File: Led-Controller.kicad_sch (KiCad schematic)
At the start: 68 parts, among them J1 Program, J2 Barrel_Jack, J3 Screw_Terminal, Q1 CSD18540Q5B, Q2 CSD18540Q5B, Q3 CSD18540Q5B, Q4 CSD18540Q5B, Q5 CSD18540Q5B, Q6 CSD18540Q5B, U1 TPS5430DDA, U2 TPS5430DDA, U3 ESP32-WROOM-32E, U4 1ED44175N01BXTSA1, U5 1ED44175N01BXTSA1, U6 1ED44175N01BXTSA1, U7 1ED44175N01BXTSA1, U8 1ED44175N01BXTSA1

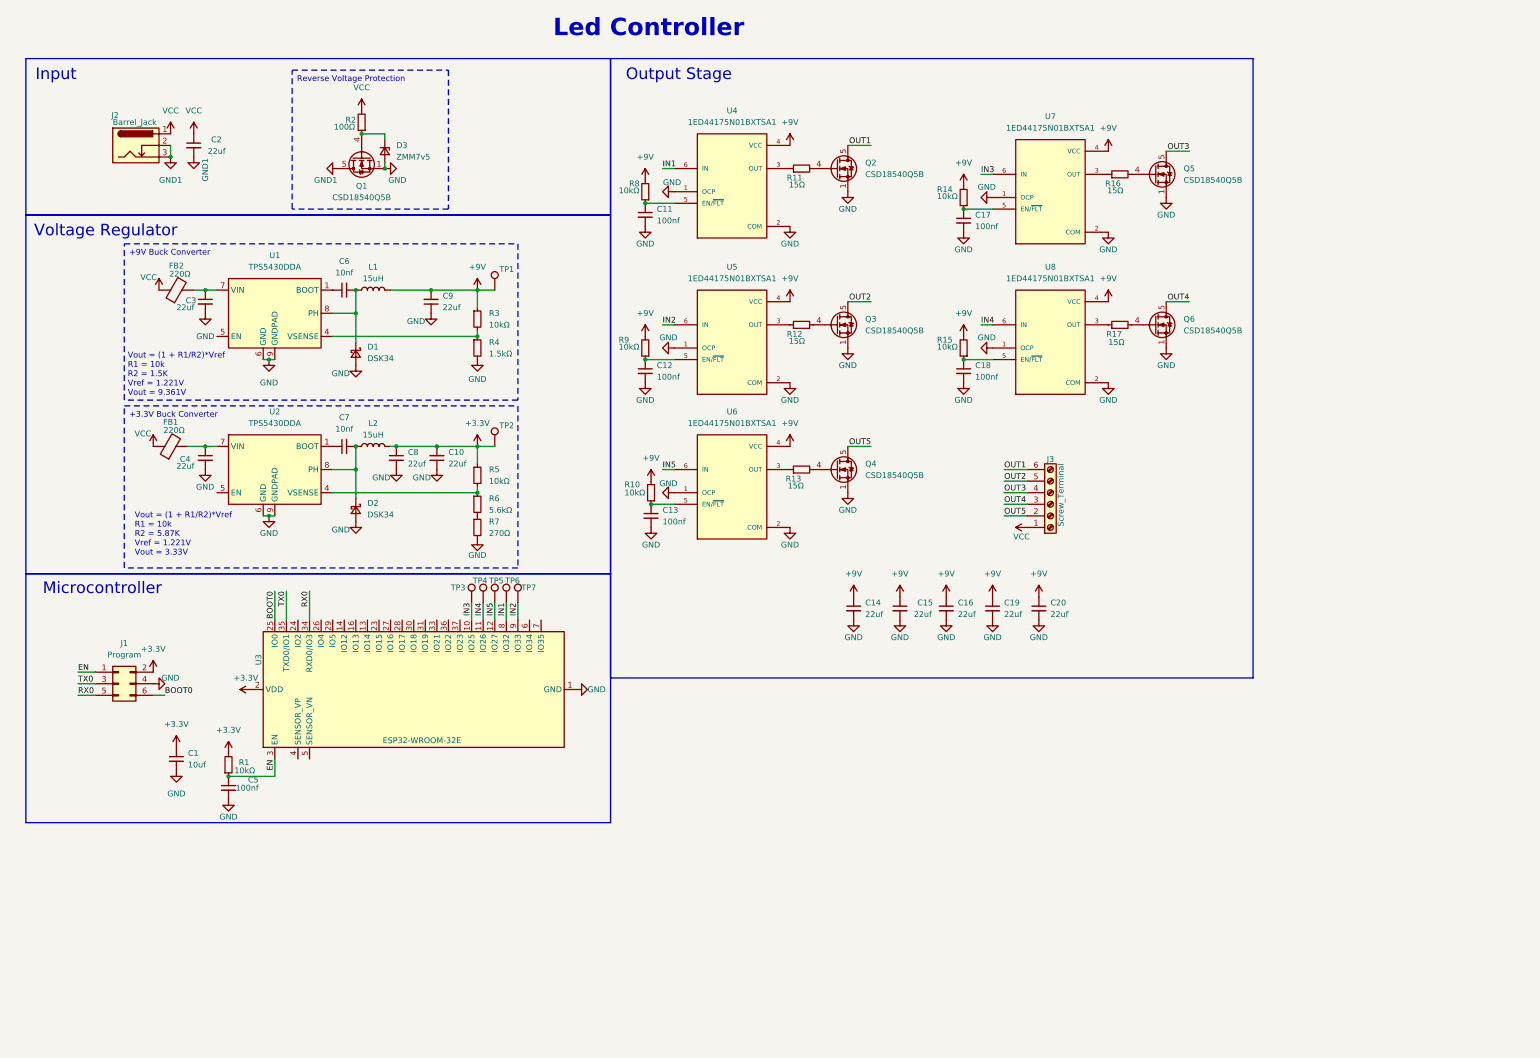
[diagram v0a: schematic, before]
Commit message: Added: New power stage
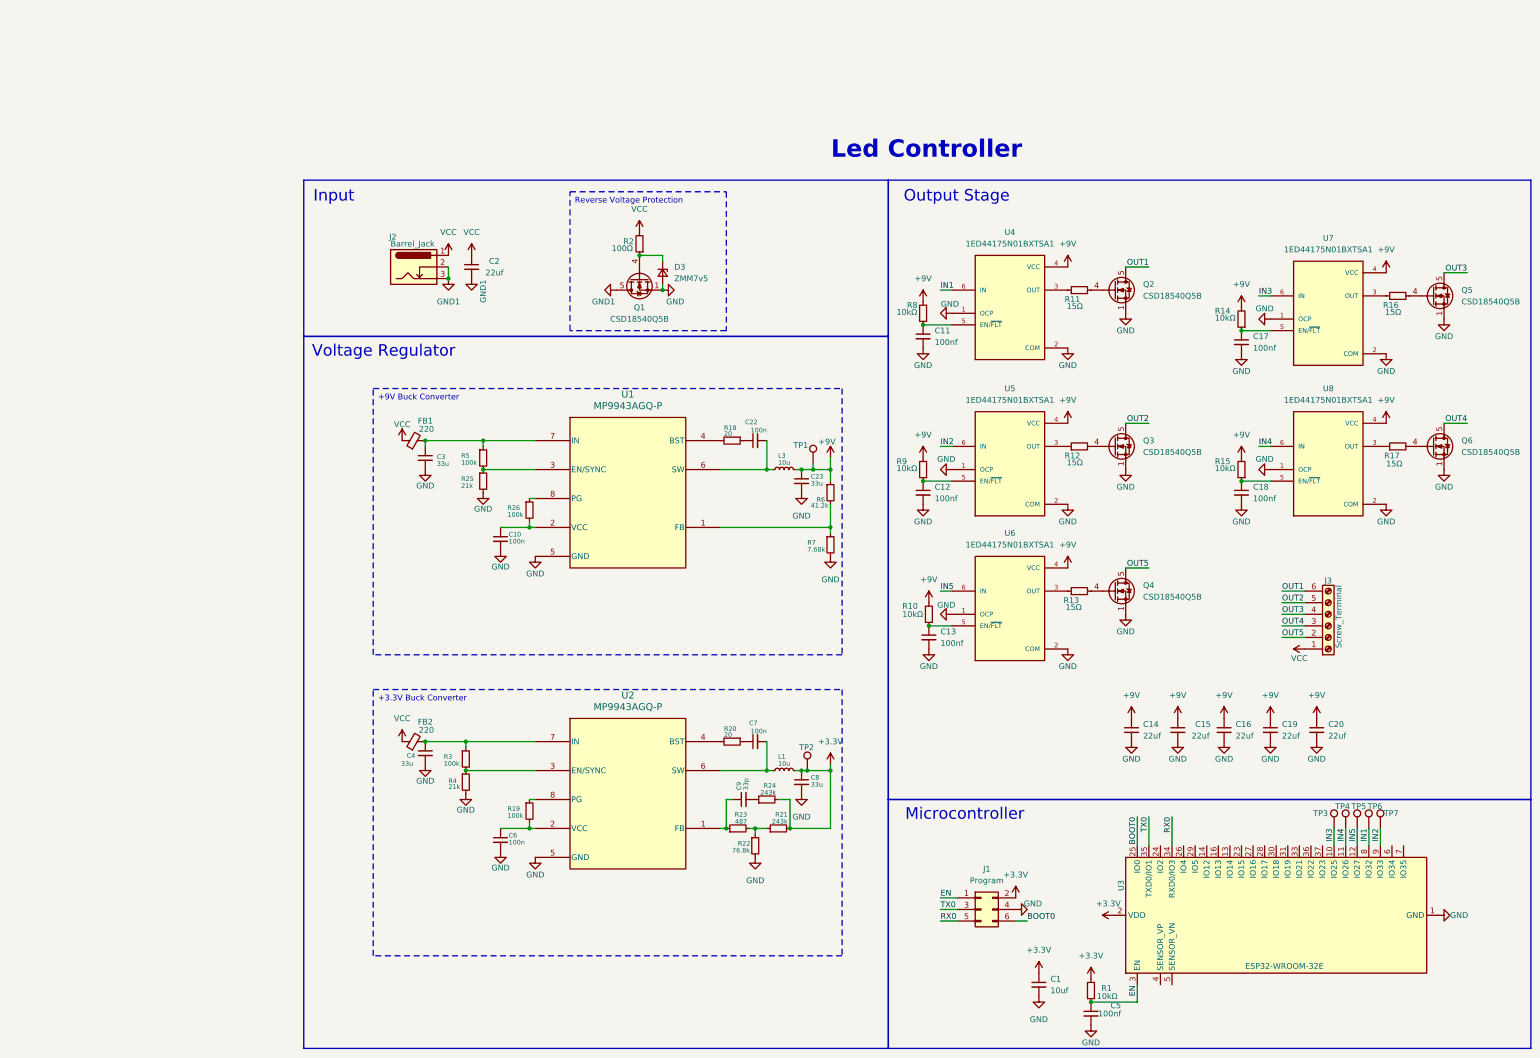
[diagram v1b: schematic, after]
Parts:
- removed D1, D2: DSK34, Diode_SMD:D_SOD-123, symbol Device:D_Schottky_Small
- removed FB1, FB2: 220Ω, Resistor_SMD:R_0805_2012Metric, symbol Device:FerriteBead
- removed L1, L2: 15uH, Inductor_SMD:L_Bourns-SRN8040_8x8.15mm, symbol Device:L
- removed TP1: ~, TestPoint:TestPoint_Pad_D1.0mm, symbol Connector:TestPoint
- removed U1, U2: TPS5430DDA, Package_SO:TI_SO-PowerPAD-8_ThermalVias, symbol Regulator_Switching:TPS5430DDA
- added C22: 100n, Capacitor_SMD:C_0603_1608Metric, symbol Device:C_Small
- added C23: 33u, Capacitor_SMD:C_0603_1608Metric, symbol Device:C_Small
- added FB1, FB2: 220, Inductor_SMD:L_0603_1608Metric, symbol Device:FerriteBead_Small
- added L1, L3: 10u, Inductor_SMD:L_Taiyo-Yuden_MD-5050, symbol Device:L_Small
- added R18, R20: 20, Resistor_SMD:R_0603_1608Metric, symbol Device:R_Small
- added R19, R26: 100k, Resistor_SMD:R_0603_1608Metric, symbol Device:R_Small
- added R21, R24: 243k, Resistor_SMD:R_0603_1608Metric, symbol Device:R_Small
- added R22: 76.8k, Resistor_SMD:R_0603_1608Metric, symbol Device:R_Small
- added R23: 487, Resistor_SMD:R_0603_1608Metric, symbol Device:R_Small
- added R25: 21k, Resistor_SMD:R_0603_1608Metric, symbol Device:R_Small
- added TP2: ~, TestPoint:TestPoint_Pad_D1.0mm, symbol Connector:TestPoint
- added U1, U2: MP9943AGQ-P, MP9943A:MP9943A, symbol MP9943A:MP9943AGQ-P
- C10: value 22uf -> 100n; footprint Capacitor_SMD:C_0805_2012Metric -> Capacitor_SMD:C_0603_1608Metric; Package 805 -> (none)
- C3, C4, C8: value 22uf -> 33u; footprint Capacitor_SMD:C_0805_2012Metric -> Capacitor_SMD:C_0603_1608Metric; Package 805 -> (none)
- C6, C7: value 10nf -> 100n; footprint Capacitor_SMD:C_0402_1005Metric -> Capacitor_SMD:C_0603_1608Metric; Package 402 -> (none)
- C9: value 22uf -> 33p; footprint Capacitor_SMD:C_0805_2012Metric -> Capacitor_SMD:C_0603_1608Metric; Package 805 -> (none)
- R3, R5: value 10kΩ -> 100k; footprint Resistor_SMD:R_0402_1005Metric -> Resistor_SMD:R_0603_1608Metric; MANUFACTURER Any -> (none); Package 402 -> (none)
- R4: value 1.5kΩ -> 21k; footprint Resistor_SMD:R_0402_1005Metric -> Resistor_SMD:R_0603_1608Metric; MANUFACTURER Any -> (none); Package 402 -> (none)
- R6: value 5.6kΩ -> 41.2k; footprint Resistor_SMD:R_0402_1005Metric -> Resistor_SMD:R_0603_1608Metric; MANUFACTURER Any -> (none); Package 402 -> (none)
- R7: value 270Ω -> 7.68k; footprint Resistor_SMD:R_0402_1005Metric -> Resistor_SMD:R_0603_1608Metric; MANUFACTURER Any -> (none); Package 402 -> (none)
- renumbered TP2 to TP1
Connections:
- net +3.3V: now also L1.2, R21.2, R24.2, TP2.1; no longer C10.2, R5.1, TP1.1
- net +9V: now also R6.1, TP1.1, C23.1, L3.2; no longer C9.2, R3.1
- net GND: now also C10.2, C6.2, C23.2, R22.2, R25.2, U1.5 (GND), U2.5 (GND); no longer C10.1, C9.1
- net VCC: now also FB1.1, FB2.1
- net at R3.2, R4.1: now also U2.3 (EN/SYNC)
- net at R5.2: now also R25.1, U1.3 (EN/SYNC); no longer R6.1
- net at C7.1: now also R20.1
- net at C4.1: now also R3.1, FB2.2, U2.7 (IN)
- net at C7.2: now also L1.1, U2.6 (SW)
- net at C3.1: now also R5.1, FB1.2, U1.7 (IN)
- net at R6.2, R7.1: now also U1.1 (FB)
- net at C6.1: now also R19.2, U2.2 (VCC)
- new net: C9.1, R23.1, U2.1 (FB)
- new net: C9.2, R24.1
- new net: R21.1, R22.1, R23.2
- new net: C22.2, L3.1, U1.6 (SW)
- new net: R20.2, U2.4 (BST)
- new net: R19.1, U2.8 (PG)
- new net: C22.1, R18.1
- new net: R18.2, U1.4 (BST)
- new net: R26.1, U1.8 (PG)
- new net: C10.1, R26.2, U1.2 (VCC)
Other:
- note removed: "Vout = (1 + R1/R2)*Vref R1 = 10k R2 = 1.5K Vref = 1.221V Vout = 9.361V"
- note removed: "Vout = (1 + R1/R2)*Vref R1 = 10k R2 = 5.87K Vref = 1.221V Vout = 3.33V"
- moved on the sheet: C1, C11, C12, C13, C14, C15, C16, C17, C18, C19, C2, C20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

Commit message: Added: new Inductor
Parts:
- L1, L3: footprint Inductor_SMD:L_Taiyo-Yuden_MD-5050 -> Inductor_SMD:L_Changjiang_FNR8040S
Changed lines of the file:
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@@
 			)
 		)
-		(property "Footprint" "Inductor_SMD:L_Taiyo-Yuden_MD-5050"
+		(property "Footprint" "Inductor_SMD:L_Changjiang_FNR8040S"
 			(at 180.34 118.11 0)
 			(effects
@@
 			)
 		)
-		(property "Footprint" "Inductor_SMD:L_Taiyo-Yuden_MD-5050"
+		(property "Footprint" "Inductor_SMD:L_Changjiang_FNR8040S"
 			(at 180.34 184.15 0)
 			(effects

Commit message: review pending
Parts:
- added C21, C24: 470uf, Capacitor_THT:CP_Radial_D10.0mm_P2.50mm_P5.00mm, symbol Device:C_Polarized
- added C25, C26, C27, C28, C29, C30, C32, C33, C34, C35, C36: 100nf, Capacitor_SMD:C_0402_1005Metric, symbol Device:C_Small
- added C31: 22uf, Capacitor_SMD:C_0805_2012Metric, symbol Device:C_Small
- added J4, J6: Screw_Terminal, TerminalBlock:TerminalBlock_bornier-2_P5.08mm, symbol Connector:Screw_Terminal_01x02
- added J5: Ws2812 Conn, Connector_PinHeader_2.54mm:PinHeader_1x03_P2.54mm_Horizontal, symbol Connector_Generic:Conn_01x03
- added JP1: Jumper_3_Open, Jumper:SolderJumper-3_P2.0mm_Open_TrianglePad1.0x1.5mm, symbol Jumper:Jumper_3_Open
- added R27, R28, R29, R30, R31: 100, Resistor_SMD:R_0402_1005Metric, symbol Device:R_Small
- added R33: 37.4k, Resistor_SMD:R_0603_1608Metric, symbol Device:R_Small
- added TP8: ~, TestPoint:TestPoint_Pad_D1.0mm, symbol Connector:TestPoint
- added U9: SN74LV1T34DBV, Package_TO_SOT_SMD:SOT-23-5, symbol Logic_LevelTranslator:SN74LV1T34DBV
- J1: footprint Connector_PinHeader_1.27mm:PinHeader_2x03_P1.27mm_Vertical -> Connector_PinHeader_2.54mm:PinHeader_2x03_P2.54mm_Vertical
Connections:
- net +9V: now also C25.1, C26.1, C27.1, C28.1, C29.1, JP1.1 (A)
- net GND: now also C21.2, C24.2, C25.2, C26.2, C27.2, C28.2, C29.2, C30.2, C31.2, C32.2, C33.2, C34.2, C35.2, C36.2, J5.3 (Pin_3), J6.1 (Pin_1), U9.3 (GND)
- net GND1: now also J4.1 (Pin_1)
- net OUT1: now also R27.2
- net OUT2: now also R28.2
- net OUT3: now also R29.2
- net OUT4: now also R30.2
- net OUT5: now also R31.2
- net VCC: now also C21.1, C24.1, J4.2 (Pin_2), J6.2 (Pin_2)
- net at R6.2, R7.1, U1.1 (FB): now also R33.2
- net DOUT: now reaches U3.27 (IO16)
- net DOUT: now also TP8.1, U9.2 (A)
- new net: C32.1, R27.1
- new net: C34.1, R29.1
- new net: C36.1, R31.1
- new net: JP1.2 (C), R33.1
- new net: C35.1, R30.1
- new net: J5.2 (Pin_2), U9.4 (Y)
- new net: C33.1, R28.1
- new net +5V: C30.1, C31.1, JP1.3 (B), U9.5 (VCC)
- no-connect marks 0 -> 1
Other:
- note added: "Led Controller Common +"
- note added: "Note : When using WS2812 the input supply should be 5V"
- note added: "Output Stage WS2812"
- note added: "Snubber Network"
- note added: "VDD Min : 4V (if using WS2812) VDD Min : 9V (if using RGBWWW) VDD Max : 30V"
- note removed: "Led Controller"
- moved on the sheet: C10, C14, C15, C16, C19, C20, C22, C23, C3, C4, C6, C7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

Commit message: Review done
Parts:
- added C39, C40: 33u, Capacitor_SMD:C_0603_1608Metric, symbol Device:C_Small
- added H1, H2: MountingHole, MountingHole:MountingHole_3.2mm_M3_DIN965_Pad, symbol Mechanical:MountingHole
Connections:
- net +3.3V: now also C39.1, C40.1
- net GND: now also C39.2, C40.2
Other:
- moved on the sheet: C23, L3

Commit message: WIP::Added: BOM for major components
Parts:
- removed C31: 22uf, Capacitor_SMD:C_0805_2012Metric, symbol Device:C_Small
- C1: Manufacturer (none) -> Murata Electronics; Part No (none) -> GRM155R60J106ME05J
- C10, C22, C6, C7: value 100n -> 0.1uf; Manufacturer (none) -> Murata Electronics; Package (none) -> 603; Part No (none) -> GCJ188R71C104MA01J
- C11, C12, C13, C17, C18, C32, C33, C34, C35, C36, C5: value 100nf -> 0.1uf; Manufacturer (none) -> Murata Electronics; Part No (none) -> GRM155R61C104KA88D
- C14, C15, C16, C19, C2, C20: Manufacturer (none) -> Murata Electronics; Part No (none) -> GRM21BR61C226ME44L
- C23, C3, C39, C4, C40, C8: value 33u -> 22uf; Manufacturer (none) -> Murata Electronics; Package (none) -> 603; Part No (none) -> GRM188C61C226ME01W
- C25, C26, C27, C28, C29: value 100nf -> 0.1uf; footprint Capacitor_SMD:C_0402_1005Metric -> Capacitor_SMD:C_0805_2012Metric; Manufacturer (none) -> Murata Electronics; Package 402 -> 805; Part No (none) -> GCM21BR71E104KA37L
- C30: value 100nf -> 0.1uf; footprint Capacitor_SMD:C_0402_1005Metric -> Capacitor_SMD:C_0805_2012Metric; Manufacturer (none) -> Murata Electronics; Package 402 -> 805; Part No (none) -> GCM21BR71E104KA37L; now fitted; now in the parts list
- C9: value 33p -> 33pf; Manufacturer (none) -> Murata Electronics; Package (none) -> 603; Part No (none) -> GCM1885C2A330JA16D
- D3: value ZMM7v5 -> ZMM7V5; Manufacturer (none) -> Shenzhen Slkormicro Semicon Co., Ltd.; Package (none) -> DO-213AC; Part No (none) -> ZMM7V5
- FB1, FB2, R18, R19, R20, R21, R22, R23, R24, R25, R26, R3, R33, R4, R5, R6, R7: Package (none) -> 603
- J5, J6: now fitted; now in the parts list
- L1, L3: value 10u -> 10uH
- Q1, Q2, Q3, Q4, Q5, Q6: Package TDSON 8 -> 8-VSON-CLIP (5x6); Part No (none) -> CSD18540Q5B
- R1, R10, R11, R12, R13, R14, R15, R16, R17, R2, R27, R28, R29, R30, R31, R8, R9: MANUFACTURER Any -> (none)
- TP3, TP4, TP5, TP6, TP7, TP8: now left out of the parts list
- U1, U2: Manufacturer (none) -> Monolithic Power Systems Inc.; Package (none) -> 8-QFN (3x3); Part No (none) -> MP9943AGQ-P
- U3: MANUFACTURER Espresiff -> (none); Manufacturer (none) -> Espressif Systems; Package (none) -> 38-SMD Module; Part No (none) -> ESP32-WROOM-32E-N8
- U4, U5, U6, U7, U8: Check_prices https://www.snapeda.com/parts/1ED44175N01BXTSA1/Infineon+Te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 -> (none); Description_1 Low-Side Gate Driver IC Non-Inverting PG-SOT23-6-3 -> (none); MANUFACTURER Infineon -> (none); MAXIMUM_PACKAGE_HEIGHT 1.45mm -> (none); MF Infineon Technologies -> (none); MP 1ED44175N01BXTSA1 -> (none); Manufacturer (none) -> Infineon Technologies; PARTREV 1.0 -> (none); Package SOT-23-6 Infineon Technologies -> SOT-23-6; Part No (none) -> 1ED44175N01BXTSA1; Purchase-URL https://www.snapeda.com/api/url_track_click_mouser/?unipart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 -> (none); STANDARD IPC-7351B -> (none); SnapEDA_Link https://www.snapeda.com/parts/1ED44175N01BXTSA1/Infineon+Te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 -> (none)
- U9: Manufacturer (none) -> Texas Instruments; Package (none) -> SOT-23-5; Part No (none) -> SN74LV1T34DBVR; now fitted; now in the parts list
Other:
- note added: "VDD Min : 5V (if using WS2812) VDD Min : 9V (if using RGBWWW) VDD Max : 30V"
- note removed: "VDD Min : 4V (if using WS2812) VDD Min : 9V (if using RGBWWW) VDD Max : 30V"

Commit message: review still pending , BOM finalized and changed to 0603
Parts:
- added C31: 0.1uf, Capacitor_SMD:C_0603_1608Metric, symbol Device:C_Small
- C1: footprint Capacitor_SMD:C_0402_1005Metric -> Capacitor_SMD:C_0603_1608Metric; Package 402 -> 603; Part No GRM155R60J106ME05J -> GRM188R60J106KE47D
- C11, C12, C13, C17, C18, C32, C33, C34, C35, C36, C5: footprint Capacitor_SMD:C_0402_1005Metric -> Capacitor_SMD:C_0603_1608Metric; Package 402 -> 603; Part No GRM155R61C104KA88D -> GCJ188R71C104MA01J
- C21, C24: Part No (none) -> to be choosen
- FB1, FB2: Manufacturer (none) -> Murata Electronics; Part No (none) -> BLM18RK221SN1D
- L1, L3: Manufacturer (none) -> Bourns Inc.; Part No (none) -> SRN8040-100M
- R1, R10, R14, R15, R8, R9: footprint Resistor_SMD:R_0402_1005Metric -> Resistor_SMD:R_0603_1608Metric; Package 402 -> 603; Part No (none) -> RC0603FR-0710KL
- R11, R12, R13, R16, R17: footprint Resistor_SMD:R_0402_1005Metric -> Resistor_SMD:R_0603_1608Metric; Package 402 -> 603; Part No (none) -> RC0603FR-0715RL
- R18, R20: Part No (none) -> RC0603JR-0720RL
- R19, R26, R3, R5: Part No (none) -> RC0603FR-07100KL
- R2: footprint Resistor_SMD:R_0402_1005Metric -> Resistor_SMD:R_0603_1608Metric; Package 402 -> 603; Part No (none) -> RC0603FR-07100RL
- R21, R24: Part No (none) -> RC0603FR-07243KL
- R22: Part No (none) -> RC0603FR-0776K8L
- R23: Part No (none) -> RC0603FR-07487RL
- R25, R4: Part No (none) -> RC0603FR-0721KL
- R27, R28, R29, R30, R31: value 100 -> 100Ω; footprint Resistor_SMD:R_0402_1005Metric -> Resistor_SMD:R_0603_1608Metric; Package 402 -> 603; Part No (none) -> RC0603FR-07100RL
- R33: Part No (none) -> RC0603FR-0737K4L
- R6: Part No (none) -> RC0603FR-0742K2L
- R7: Part No (none) -> RC0603FR-077K68L
- TP1, TP2: now left out of the parts list
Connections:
- net +3.3V: now also C31.1
- net GND: now also C31.2

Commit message: Fixed::BOM: Fixed unconsistencies in BOM
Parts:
- C21, C24: Manufacturer (none) -> Rubycon; Part No to be choosen -> 35PX470MEFC10X12.5
- J1: Manufacturer (none) -> Mill-Max Manufacturing Corp.; Part No (none) -> 852-40-006-10-003000
- Q1, Q2, Q3, Q4, Q5, Q6: Manufacturer (none) -> Texas Instruments
- R1, R10, R11, R12, R13, R14, R15, R16, R17, R18, R19, R2, R20, R21, R22, R23, R24, R25, R26, R27, R28, R29, R3, R30, R31, R33, R4, R5, R6, R7, R8, R9: Manufacturer (none) -> YAGEO

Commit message: Fix::Voltage Reg and LED Pin
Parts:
- R33: value 37.4k -> 90k
- R6: value 41.2k -> 90k
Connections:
- net IN1: now also U3.37 (IO23); no longer U3.8 (IO32)
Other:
- moved on the sheet: TP6
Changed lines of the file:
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@@
 	(wire
 		(pts
+			(xy 298.45 196.85) (xy 298.45 200.66)
+		)
+		(stroke
+			(width 0)
+			(type default)
+		)
+	)
+	(wire
+		(pts
 			(xy 167.64 190.5) (xy 167.64 196.85)
 		)
@@
 	(wire
 		(pts
-			(xy 308.61 196.85) (xy 308.61 200.66)
-		)
-		(stroke
-			(width 0)
-			(type default)
-		)
-	)
-	(wire
-		(pts
 			(xy 265.43 200.66) (xy 265.43 194.31)
 		)
@@
 	)
 	(label "IN1"
-		(at 308.61 196.85 270)
+		(at 298.45 196.85 270)
 		(effects
 			(font
@@
 		(dnp no)
 		(property "Reference" "TP5"
-			(at 304.8 192.024 0)
+			(at 306.07 192.024 90)
 			(effects
 				(font
@@
 		(dnp no)
 		(property "Reference" "TP3"
-			(at 296.418 193.548 0)
+			(at 300.99 192.024 90)
 			(effects
 				(font
@@
 			)
 		)
-		(property "Value" "41.2k"
+		(property "Value" "90k"
 			(at 172.212 125.984 0)
 			(effects
@@
 			)
 		)
-		(property "Value" "37.4k"
+		(property "Value" "90k"
 			(at 184.912 126.238 0)
 			(effects
@@
 	(symbol
 		(lib_id "Connector:TestPoint")
-		(at 308.61 196.85 0)
+		(at 298.45 196.85 0)
 		(unit 1)
 		(exclude_from_sim no)
@@
 		(dnp no)
 		(property "Reference" "TP6"
-			(at 308.356 192.024 0)
+			(at 298.704 192.024 90)
 			(effects
 				(font
@@
 		)
 		(property "Value" "~"
-			(at 311.15 194.8179 0)
+			(at 300.99 194.8179 0)
 			(effects
 				(font
@@
 		)
 		(property "Footprint" "TestPoint:TestPoint_Pad_D1.0mm"
-			(at 313.69 196.85 0)
+			(at 303.53 196.85 0)
 			(effects
 				(font
@@
 		)
 		(property "Datasheet" "~"
-			(at 313.69 196.85 0)
+			(at 303.53 196.85 0)
 			(effects
 				(font
@@
 		)
 		(property "Description" "test point"
-			(at 308.61 196.85 0)
+			(at 298.45 196.85 0)
 			(effects
 				(font
@@
 		)
 		(property "Manufacturer" ""
-			(at 308.61 196.85 0)
+			(at 298.45 196.85 0)
 			(effects
 				(font
@@
 		)
 		(property "Part No" ""
-			(at 308.61 196.85 0)
+			(at 298.45 196.85 0)
 			(effects
 				(font
@@
 		(dnp no)
 		(property "Reference" "TP7"
-			(at 311.912 193.548 0)
+			(at 310.896 192.024 90)
 			(effects
 				(font
@@
 		(dnp no)
 		(property "Reference" "TP4"
-			(at 301.244 192.024 0)
+			(at 303.53 192.024 90)
 			(effects
 				(font
